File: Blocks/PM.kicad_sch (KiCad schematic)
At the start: 4 parts, among them J4 TC0203620000G, J5 TC0203620000G, J6 TC0203620000G, J7 TC0203620000G

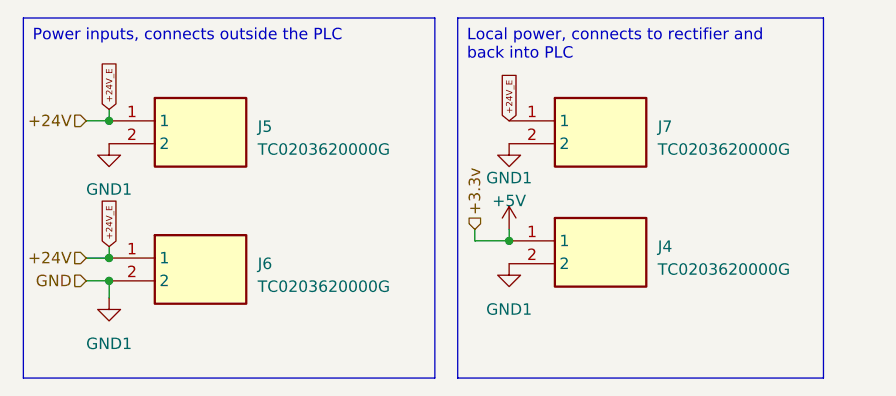
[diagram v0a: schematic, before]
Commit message: Automate library addition * Added script to automagically extract samacsys libraries and put them in corresponding folders. * Note: Requires zsh
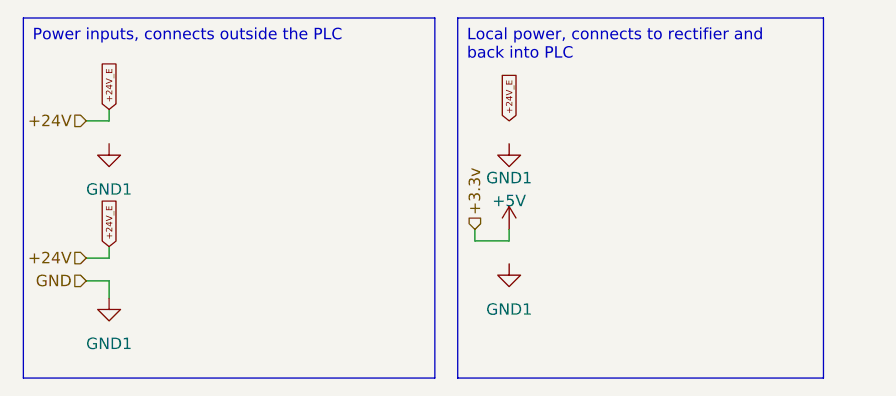
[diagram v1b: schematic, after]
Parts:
- removed J4, J5, J6, J7: TC0203620000G, TC0203620000G:TC0203620000G, symbol TC0203620000G:TC0203620000G
